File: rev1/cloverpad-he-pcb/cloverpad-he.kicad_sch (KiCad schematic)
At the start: 51 parts, among them J1 USB_C_Receptacle_USB2.0, SW1 SW_Push, SW2 SW_Push, U1 SRV05-4, U2 XC6206P332MR, U3 DRV5056A4xDBZxQ1, U4 DRV5056A4xDBZxQ1, U5 DRV5056A4xDBZxQ1, U8 RP2040, U9 W25Q16JVSSIQ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

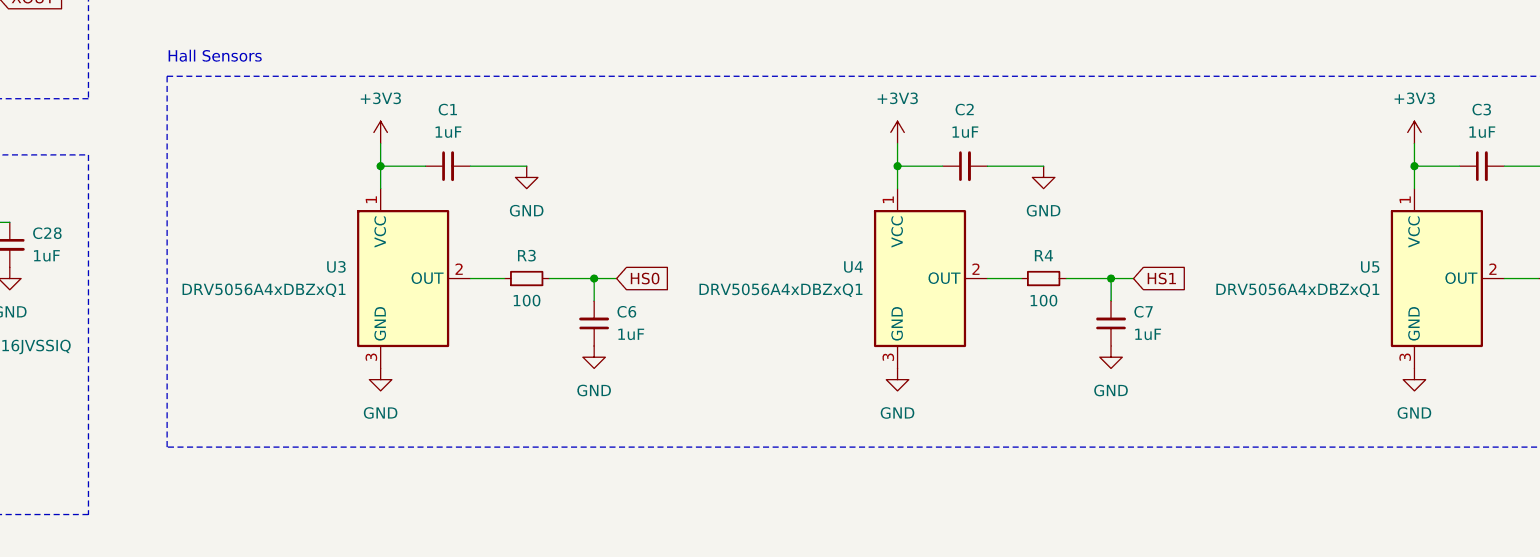
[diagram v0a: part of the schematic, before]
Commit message: fix: use DRV5056A3 instead of A4
after some testing, losing the bottom 0.2mm of travel isn't a huge problem, and it's better to increase the resolution for the upper part of the keystroke instead.
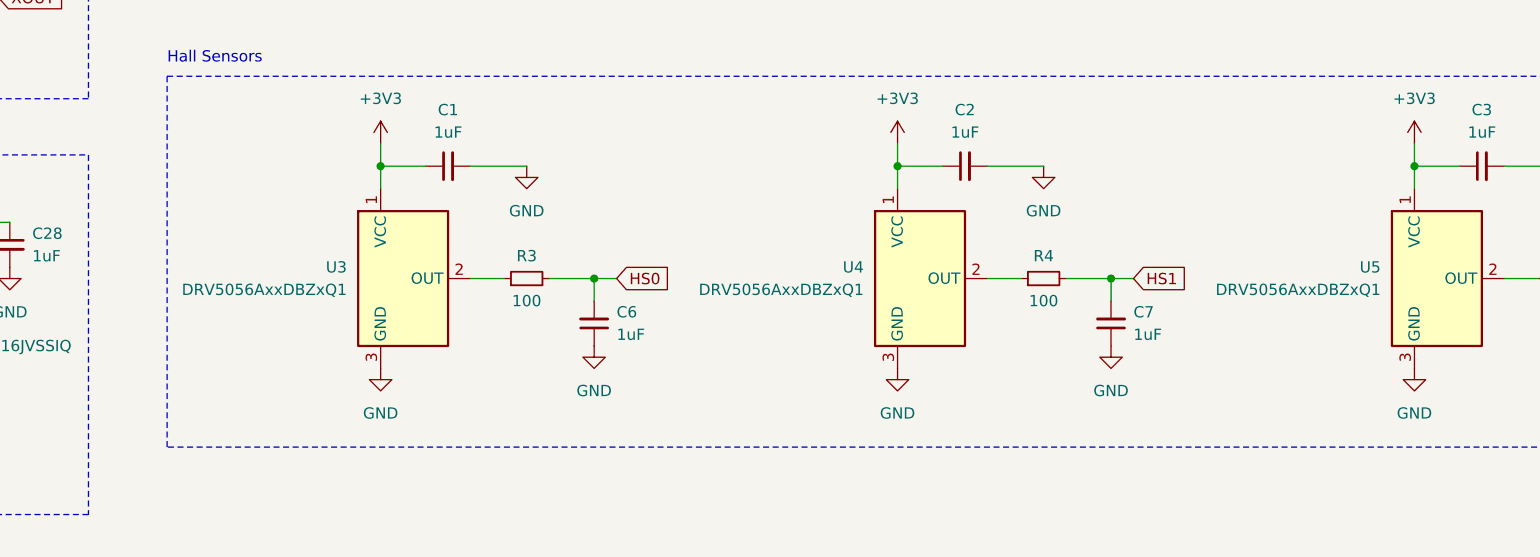
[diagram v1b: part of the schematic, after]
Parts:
- U3, U4, U5: value DRV5056A4xDBZxQ1 -> DRV5056AxxDBZxQ1; footprint Custom:KS-20-1U-DRV5056 -> Package_TO_SOT_SMD:SOT-23; symbol Custom:DRV5056A4xDBZxQ1 -> Custom:DRV5056AxxDBZxQ1; LCSC C2152902 -> C2152965
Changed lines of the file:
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@@
 	)
 	(symbol
-		(lib_id "Custom:DRV5056A4xDBZxQ1")
+		(lib_id "Custom:DRV5056AxxDBZxQ1")
 		(at 189.23 158.75 0)
 		(unit 1)
@@
 		(fields_autoplaced yes)
 		(property "Reference" "U3"
-			(at 182.88 157.48 0)
+			(at 182.88 157.4799 0)
 			(effects
 				(font
@@
 			)
 		)
-		(property "Value" "DRV5056A4xDBZxQ1"
-			(at 182.88 160.02 0)
+		(property "Value" "DRV5056AxxDBZxQ1"
+			(at 182.88 160.0199 0)
 			(effects
 				(font
@@
 			)
 		)
-		(property "Footprint" "Custom:KS-20-1U-DRV5056"
+		(property "Footprint" "Package_TO_SOT_SMD:SOT-23"
 			(at 189.23 158.75 0)
 			(effects
@@
 			)
 		)
-		(property "Description" ""
+		(property "Description" "20/39/79/158-mT, 20-kHz, 3.3/5V, SOT-23"
 			(at 189.23 158.75 0)
 			(effects
@@
 			)
 		)
-		(property "LCSC" "C2152902"
+		(property "LCSC" "C2152965"
 			(at 189.23 158.75 0)
 			(effects
@@
 	)
 	(symbol
-		(lib_id "Custom:DRV5056A4xDBZxQ1")
+		(lib_id "Custom:DRV5056AxxDBZxQ1")
 		(at 306.07 158.75 0)
 		(unit 1)
@@
 		(fields_autoplaced yes)
 		(property "Reference" "U5"
-			(at 299.72 157.48 0)
+			(at 299.72 157.4799 0)
 			(effects
 				(font
@@
 			)
 		)
-		(property "Value" "DRV5056A4xDBZxQ1"
-			(at 299.72 160.02 0)
+		(property "Value" "DRV5056AxxDBZxQ1"
+			(at 299.72 160.0199 0)
 			(effects
 				(font
@@
 			)
 		)
-		(property "Footprint" "Custom:KS-20-1U-DRV5056"
+		(property "Footprint" "Package_TO_SOT_SMD:SOT-23"
 			(at 306.07 158.75 0)
 			(effects
@@
 			)
 		)
-		(property "Description" ""
+		(property "Description" "20/39/79/158-mT, 20-kHz, 3.3/5V, SOT-23"
 			(at 306.07 158.75 0)
 			(effects
@@
 			)
 		)
-		(property "LCSC" "C2152902"
+		(property "LCSC" "C2152965"
 			(at 306.07 158.75 0)
 			(effects
@@
 	)
 	(symbol
-		(lib_id "Custom:DRV5056A4xDBZxQ1")
+		(lib_id "Custom:DRV5056AxxDBZxQ1")
 		(at 247.65 158.75 0)
 		(unit 1)
@@
 		(fields_autoplaced yes)
 		(property "Reference" "U4"
-			(at 241.3 157.48 0)
+			(at 241.3 157.4799 0)
 			(effects
 				(font
@@
 			)
 		)
-		(property "Value" "DRV5056A4xDBZxQ1"
-			(at 241.3 160.02 0)
+		(property "Value" "DRV5056AxxDBZxQ1"
+			(at 241.3 160.0199 0)
 			(effects
 				(font
@@
 			)
 		)
-		(property "Footprint" "Custom:KS-20-1U-DRV5056"
+		(property "Footprint" "Package_TO_SOT_SMD:SOT-23"
 			(at 247.65 158.75 0)
 			(effects
@@
 			)
 		)
-		(property "Description" ""
+		(property "Description" "20/39/79/158-mT, 20-kHz, 3.3/5V, SOT-23"
 			(at 247.65 158.75 0)
 			(effects
@@
 			)
 		)
-		(property "LCSC" "C2152902"
+		(property "LCSC" "C2152965"
 			(at 247.65 158.75 0)
 			(effects

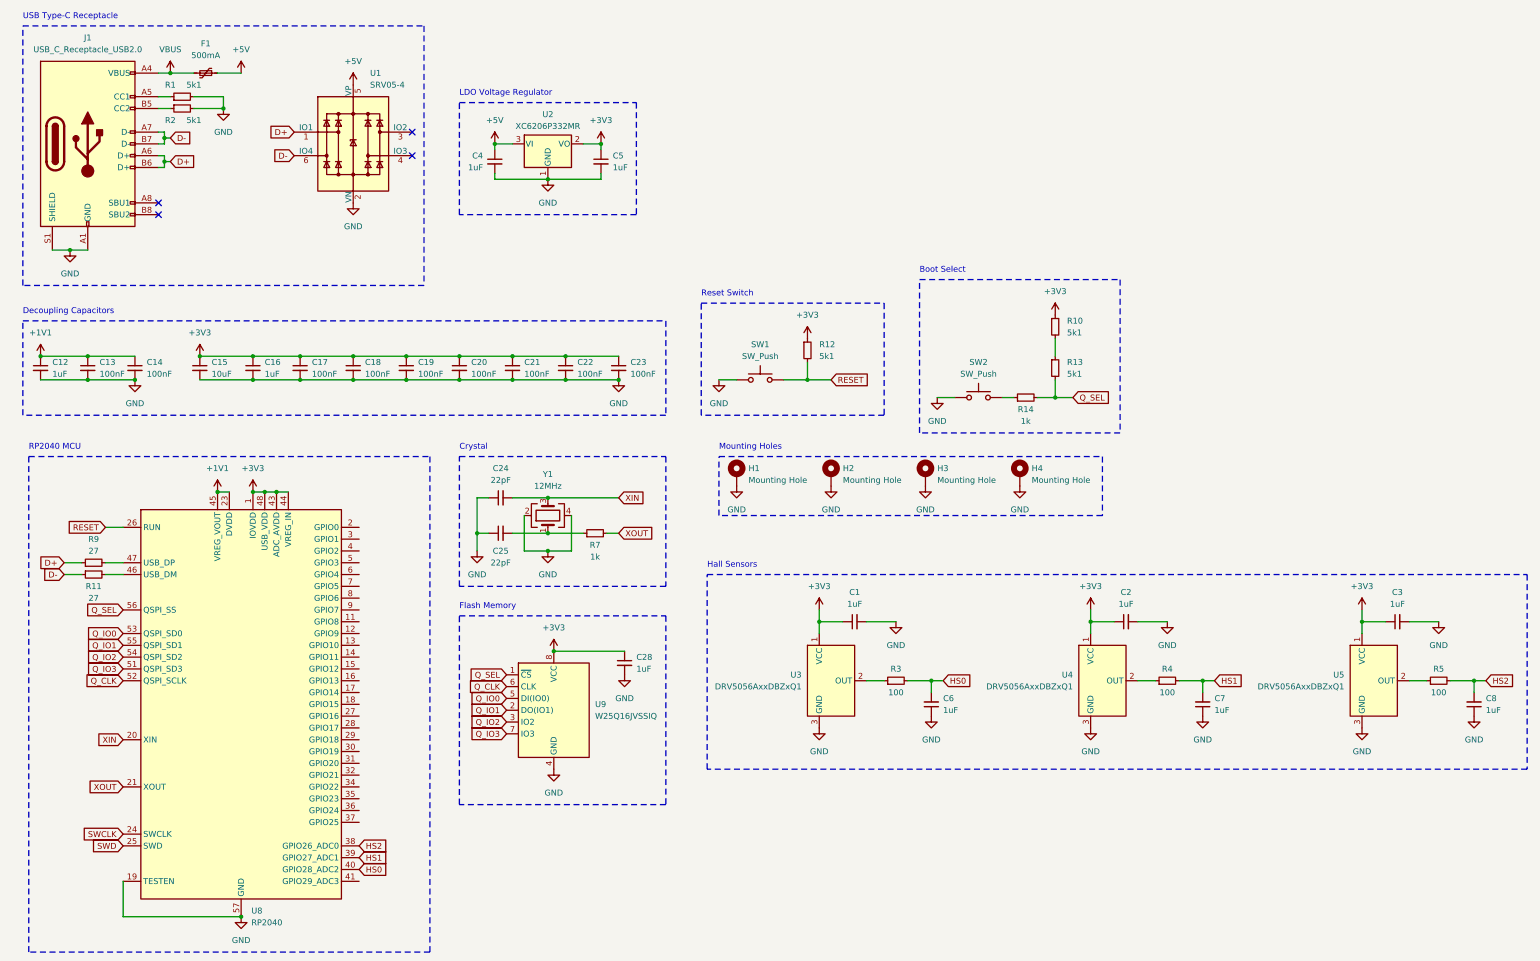
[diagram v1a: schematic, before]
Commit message: chore: update all symbols + footprints to match kicad 8
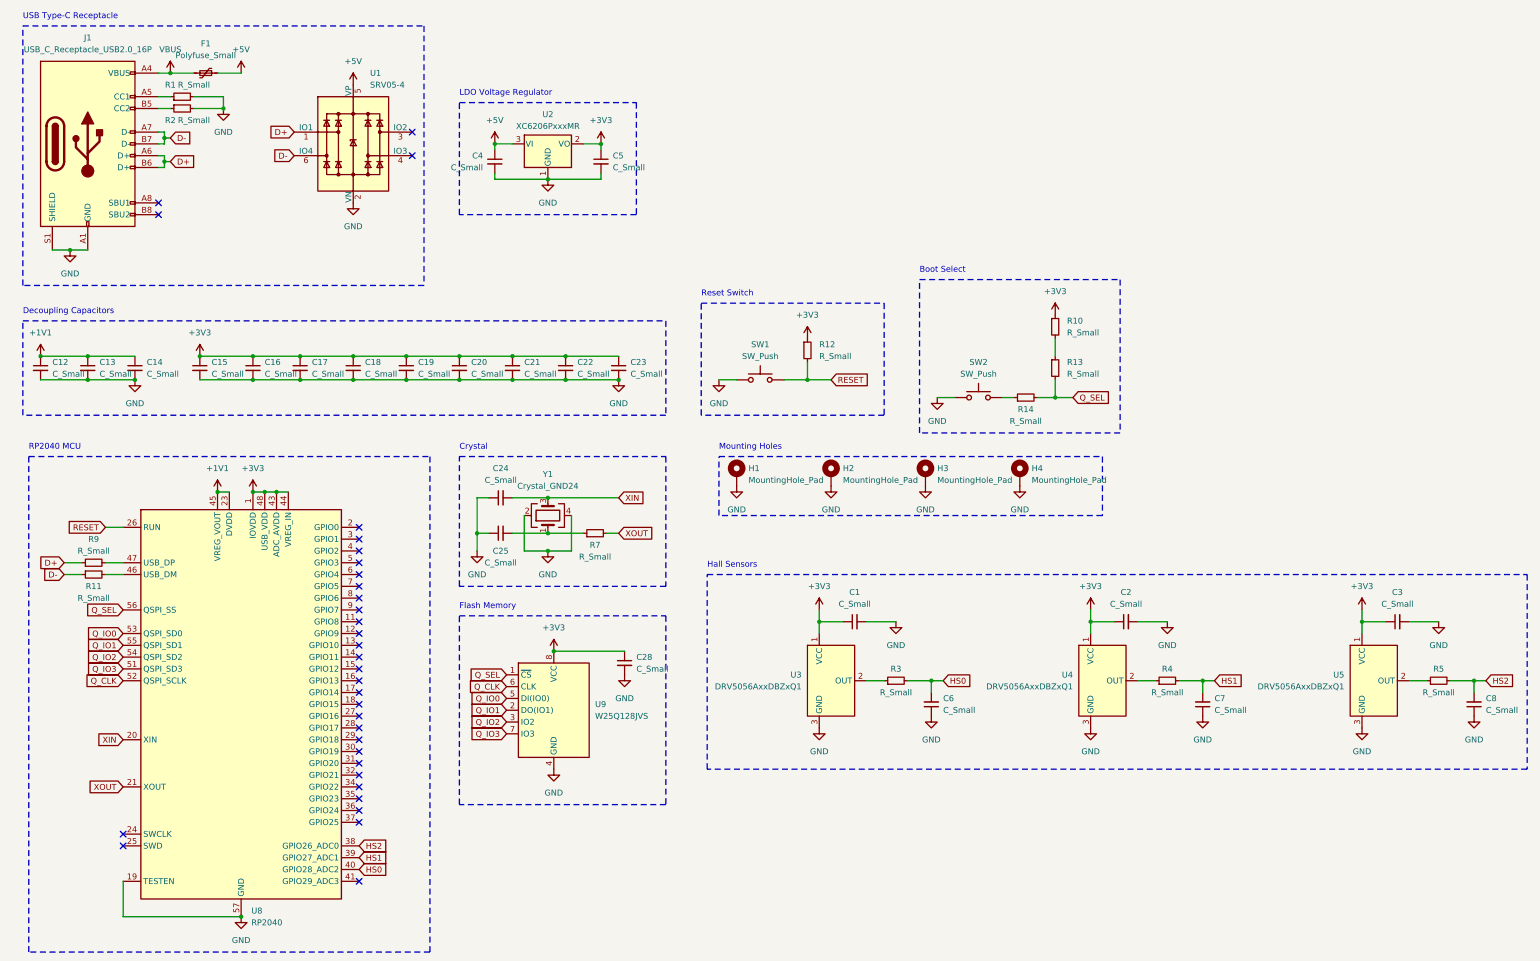
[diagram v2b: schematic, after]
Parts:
- C1, C12, C16, C2, C28, C3, C4, C5, C6, C7, C8: value 1uF -> C_Small
- C13, C14, C17, C18, C19, C20, C21, C22, C23: value 100nF -> C_Small
- C15: value 10uF -> C_Small
- C24, C25: value 22pF -> C_Small
- F1: value 500mA -> Polyfuse_Small
- H1, H2, H3, H4: value Mounting Hole -> MountingHole_Pad
- J1: value USB_C_Receptacle_USB2.0 -> USB_C_Receptacle_USB2.0_16P; symbol Connector:USB_C_Receptacle_USB2.0 -> Connector:USB_C_Receptacle_USB2.0_16P
- R1, R10, R12, R13, R2: value 5k1 -> R_Small
- R11, R9: value 27 -> R_Small
- R14, R7: value 1k -> R_Small
- R3, R4, R5: value 100 -> R_Small
- U2: value XC6206P332MR -> XC6206PxxxMR
- U9: value W25Q16JVSSIQ -> W25Q128JVS
- Y1: value 12MHz -> Crystal_GND24
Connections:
- net SWCLK: no longer names the net of U8.24 (SWCLK)
- net SWD: no longer names the net of U8.25 (SWD)
- no-connect marks 4 -> 33
